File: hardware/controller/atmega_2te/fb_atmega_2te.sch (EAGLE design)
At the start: 51 parts, among them IC1 ATMEGA 328P/168P, IC2 MC34063AP, Q1 8 MHz, T1 BC557, T2 BC547, T3 BC640

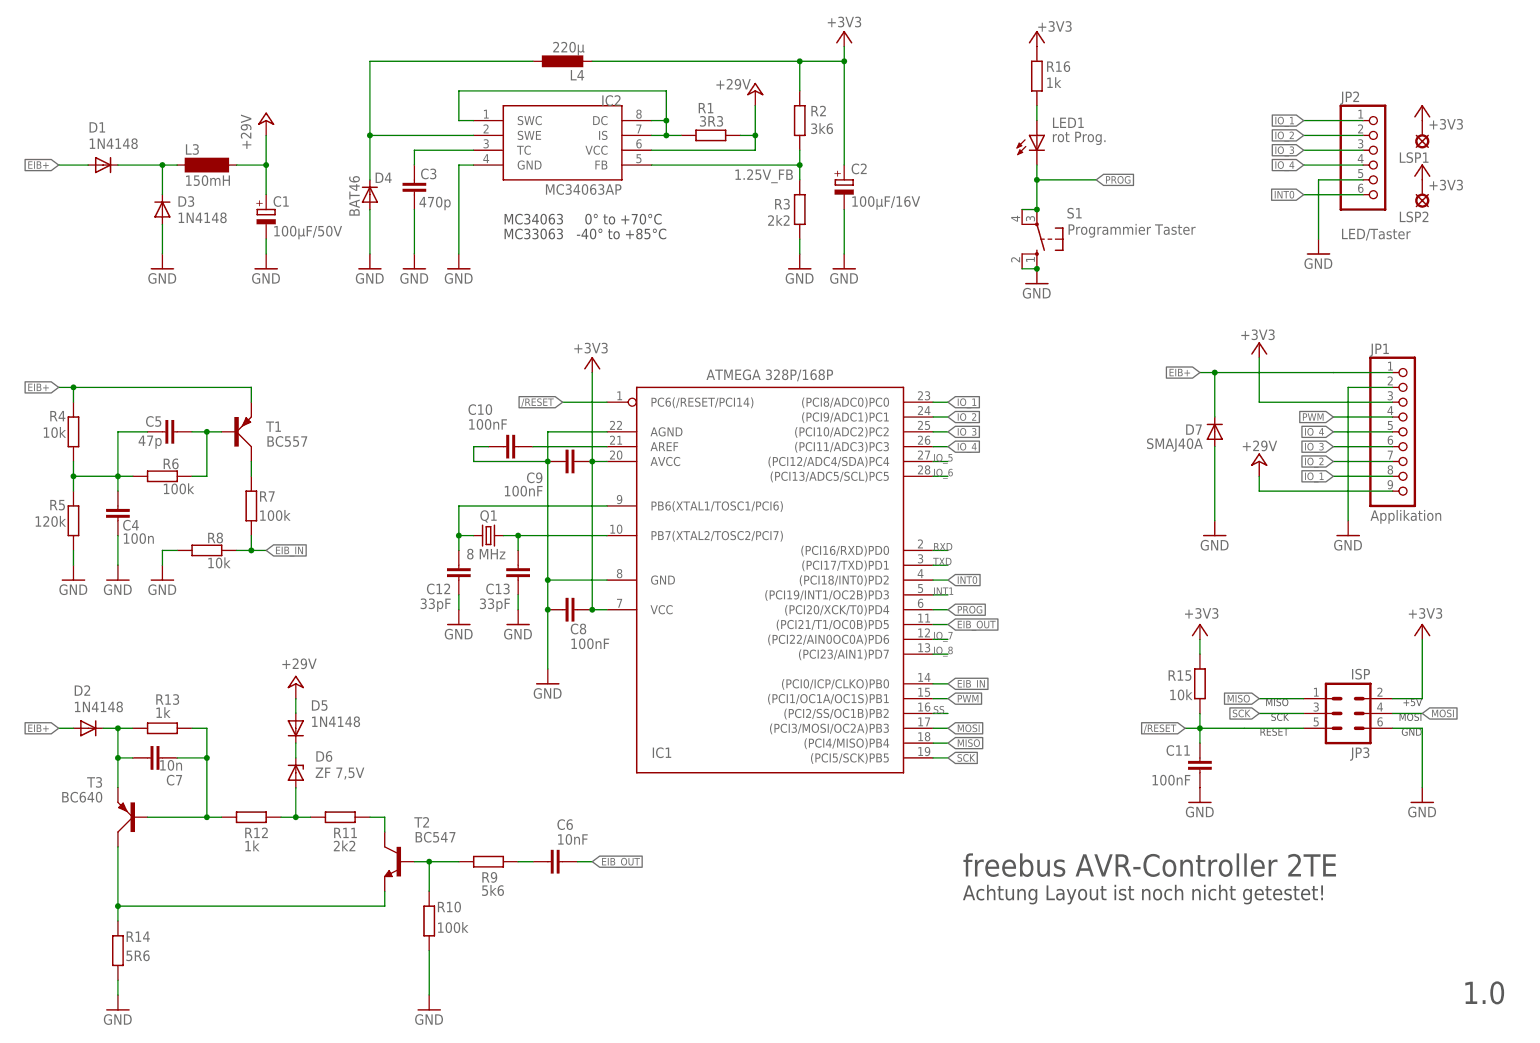
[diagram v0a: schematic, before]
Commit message: Upgraded fb_atmega_2te to version 1.1
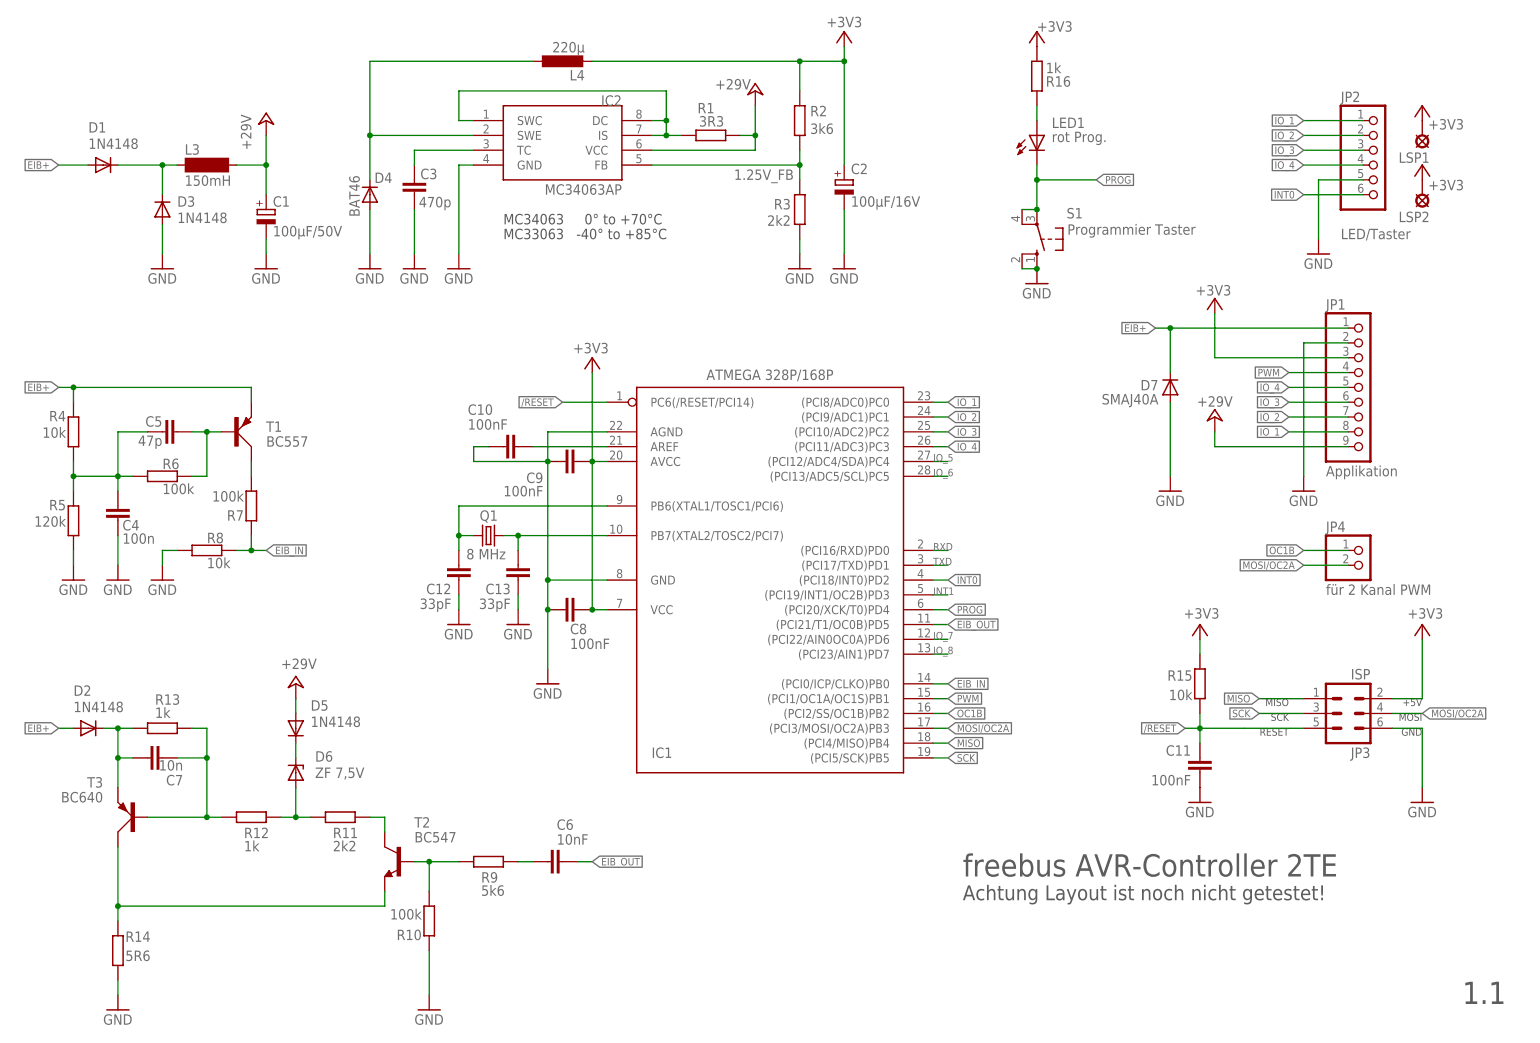
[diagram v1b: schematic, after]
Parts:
- added JP4: für 2 Kanal PWM, pinhead:PINHD-1X2
- C12, C13: device rcl:C-EU025-024X044 -> rcl:C-EUC0805
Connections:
- removed net MOSI: IC1.(PCI3/MOSI/OC2A)PB3, JP3.4
- removed net SS: IC1.(PCI2/SS/OC1B)PB2
- new net MOSI/OC2A: IC1.(PCI3/MOSI/OC2A)PB3, JP3.4, JP4.2
- new net OC1B: IC1.(PCI2/SS/OC1B)PB2, JP4.1
- net +3V3: now also R16.2; no longer R16.1
- net EIB_IN: now also R7.2; no longer R7.1
- net GND: now also R10.2; no longer R10.1
- net N$14: now also R7.1; no longer R7.2
- net N$20: now also R10.1; no longer R10.2
- net N$9: now also R16.1; no longer R16.2
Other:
- note added: "1.1"
- note removed: "1.0"
- moved on the sheet: D7, JP1, R10, R16, R7

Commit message: Upgraded fb_atmega_2te to version 1.2
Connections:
- net +3V3: now also L4.1; no longer L4.2
- net N$26: now also L4.2; no longer L4.1
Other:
- note added: "1.2"
- note removed: "1.1"
- note removed: "Achtung Layout ist noch nicht getestet!"
- moved on the sheet: L4
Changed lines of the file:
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@@
 <?xml version="1.0" encoding="utf-8"?>
 <!DOCTYPE eagle SYSTEM "eagle.dtd">
-<eagle version="6.4">
+<eagle version="6.3">
 <drawing>
 <settings>
@@
 <text x="88.9" y="137.16" size="1.778" layer="97">MC33063   -40° to +85°C</text>
 <text x="167.64" y="27.94" size="3.81" layer="97">freebus AVR-Controller 2TE</text>
-<text x="167.64" y="23.876" size="2.54" layer="97">Achtung Layout ist noch nicht getestet!</text>
-<text x="253.238" y="6.096" size="3.81" layer="97">1.1</text>
+<text x="253.238" y="6.096" size="3.81" layer="97">1.2</text>
 </plain>
 <instances>
@@
 <instance part="GND9" gate="1" x="30.48" y="78.74"/>
 <instance part="L3" gate="G$1" x="38.1" y="149.86"/>
-<instance part="L4" gate="G$1" x="99.06" y="167.64" rot="R90"/>
+<instance part="L4" gate="G$1" x="99.06" y="167.64" rot="R270"/>
 <instance part="Q1" gate="G$1" x="86.36" y="86.36" smashed="yes">
 <attribute name="NAME" x="84.836" y="88.9" size="1.778" layer="95"/>
@@
 <wire x1="66.04" y1="167.64" x2="93.98" y2="167.64" width="0.1524" layer="91"/>
 <junction x="66.04" y="154.94"/>
-<pinref part="L4" gate="G$1" pin="1"/>
+<pinref part="L4" gate="G$1" pin="2"/>
 </segment>
 </net>
@@
 <junction x="139.7" y="167.64"/>
 <junction x="147.32" y="167.64"/>
-<pinref part="L4" gate="G$1" pin="2"/>
+<pinref part="L4" gate="G$1" pin="1"/>
 <pinref part="+3V3" gate="G$1" pin="+3V3"/>
 </segment>
